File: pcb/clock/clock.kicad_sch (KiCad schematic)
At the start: 13 parts

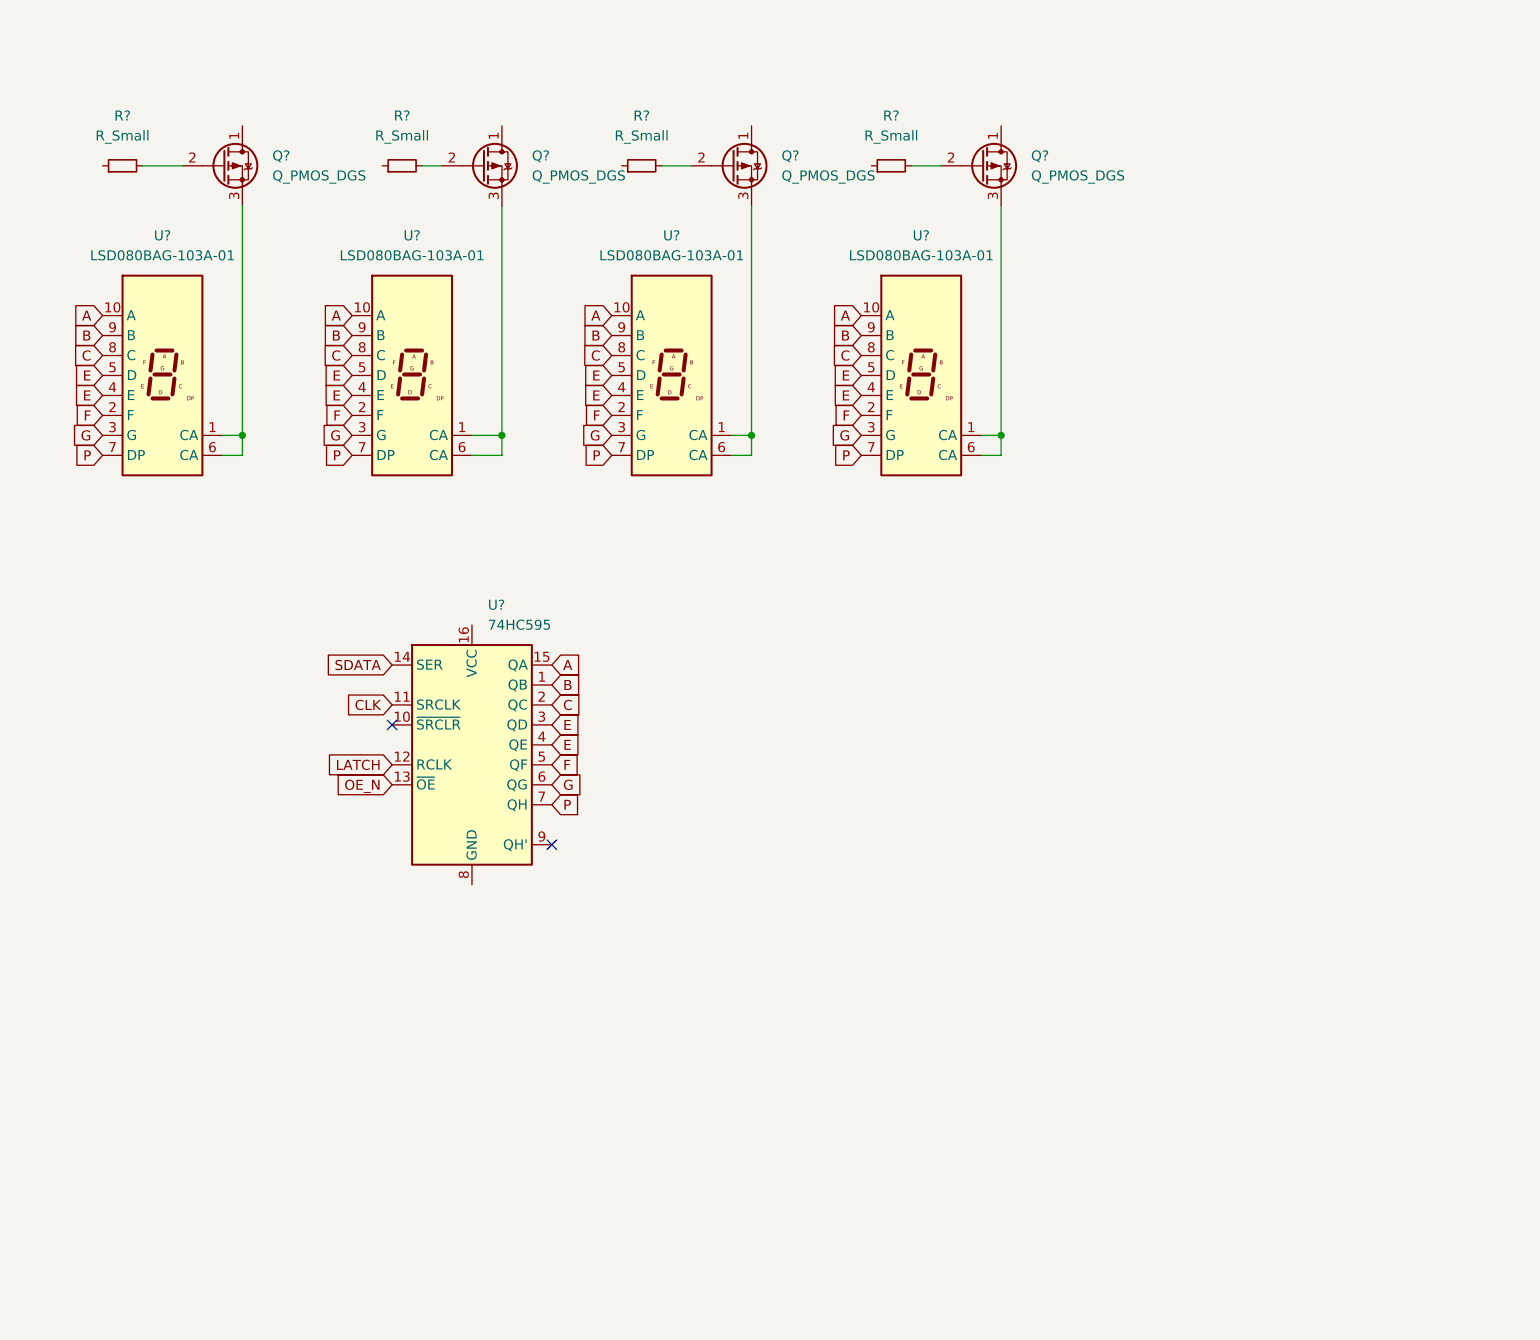
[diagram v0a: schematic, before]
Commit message: hopefully a complete schematic with footprints allocated
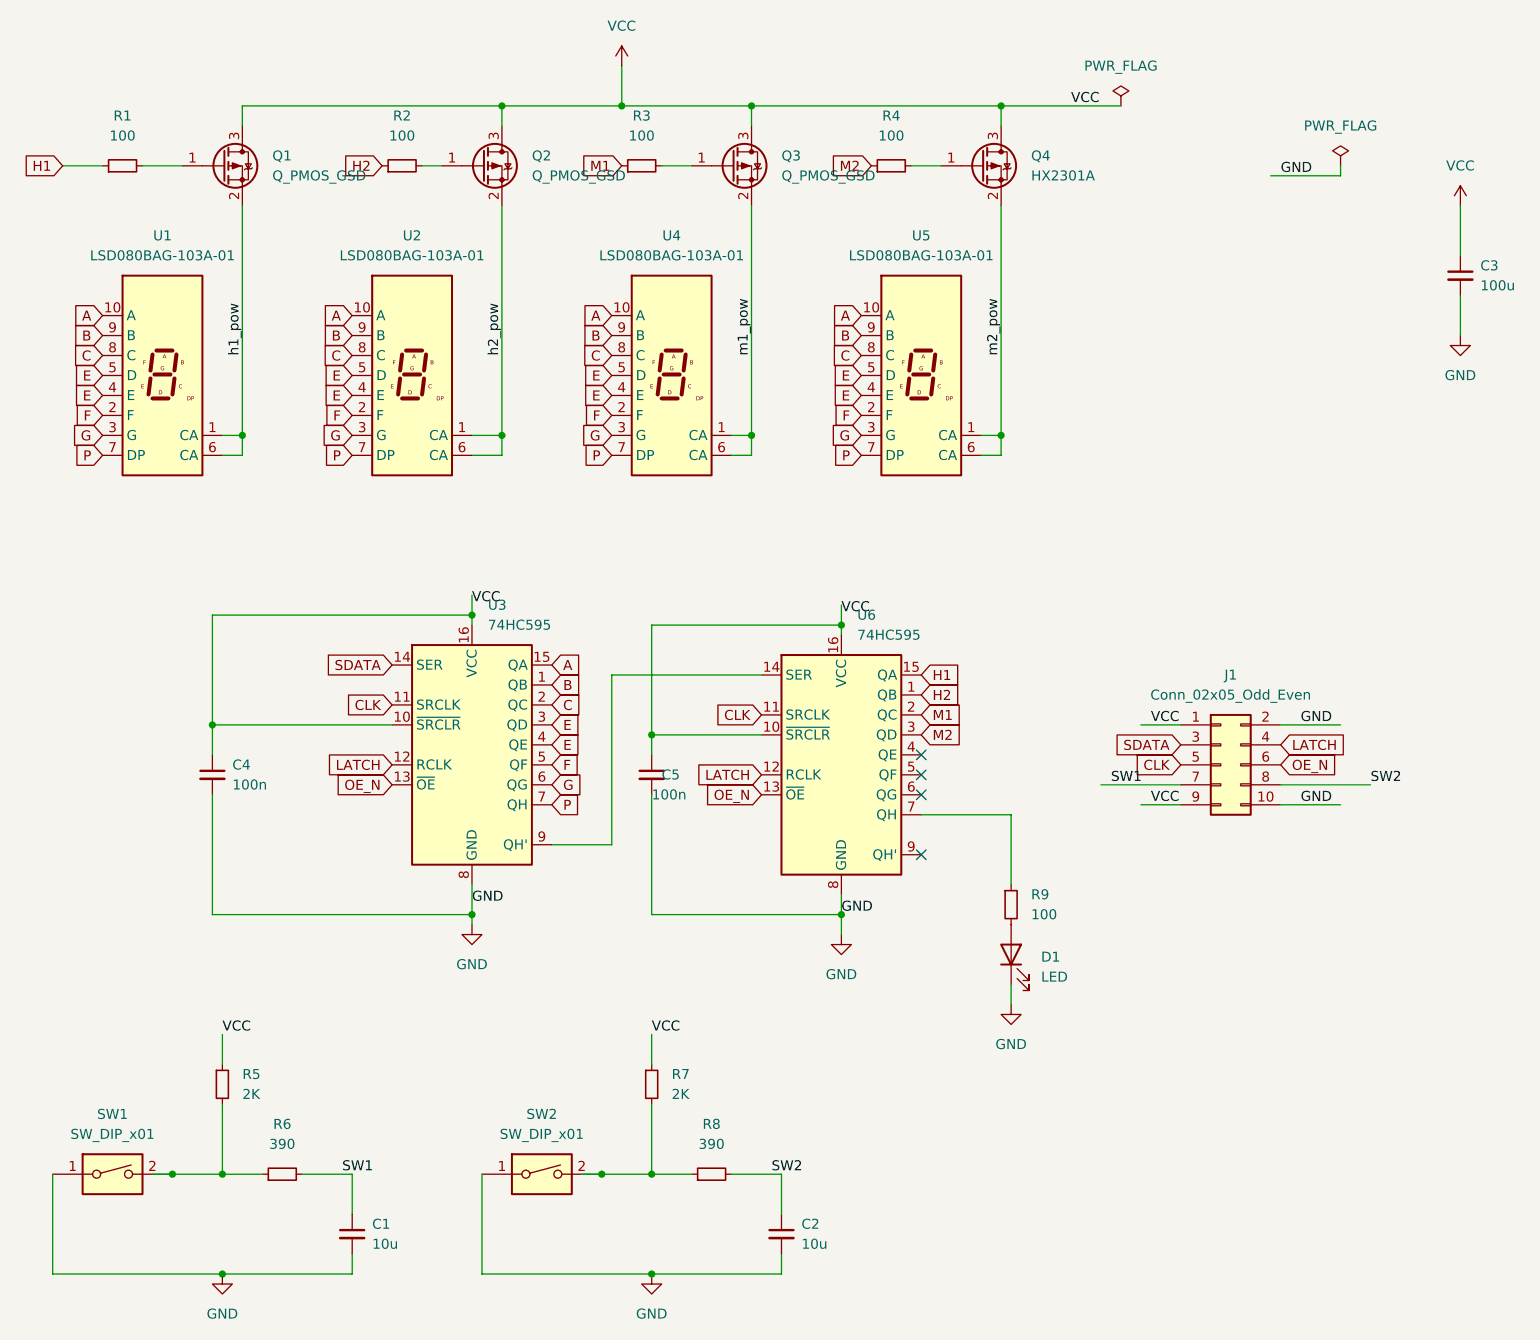
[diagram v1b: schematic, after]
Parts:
- removed Q? (x4): Q_PMOS_DGS, symbol Device:Q_PMOS_DGS
- added C1, C2: 10u, Capacitor_SMD:C_0805_2012Metric_Pad1.18x1.45mm_HandSolder, symbol Device:C_Small
- added C3: 100u, Capacitor_SMD:CP_Elec_8x10.5, symbol Device:C_Small
- added C4, C5: 100n, Capacitor_SMD:C_0805_2012Metric_Pad1.18x1.45mm_HandSolder, symbol Device:C_Small
- added D1: LED, LED_SMD:LED_0805_2012Metric_Pad1.15x1.40mm_HandSolder, symbol Device:LED
- added J1: Conn_02x05_Odd_Even, Connector_PinHeader_2.54mm:PinHeader_2x05_P2.54mm_Vertical_SMD, symbol Connector_Generic:Conn_02x05_Odd_Even
- added Q1, Q2, Q3: Q_PMOS_GSD, Package_TO_SOT_SMD:SOT-23_Handsoldering, symbol Device:Q_PMOS_GSD
- added Q4: HX2301A, Package_TO_SOT_SMD:SOT-23_Handsoldering, symbol Device:Q_PMOS_GSD
- added R5, R7: 2K, Resistor_SMD:R_0805_2012Metric_Pad1.20x1.40mm_HandSolder, symbol Device:R_Small
- added R6, R8: 390, Resistor_SMD:R_0805_2012Metric_Pad1.20x1.40mm_HandSolder, symbol Device:R_Small
- added R9: 100, Resistor_SMD:R_0805_2012Metric_Pad1.20x1.40mm_HandSolder, symbol Device:R_Small
- added SW1, SW2: SW_DIP_x01, components:SW_SPST_lcsc_c174049, symbol Switch:SW_DIP_x01
- added U6: 74HC595, Package_SO:SOIC-16_3.9x9.9mm_P1.27mm, symbol 74xx:74HC595
- R1, R2, R3, R4: renamed from R?; value R_Small -> 100; footprint (none) -> Resistor_SMD:R_0603_1608Metric_Pad0.98x0.95mm_HandSolder
- U1, U2, U4, U5: renamed from U?; footprint Display_7Segment:HDSP-7401 -> components:7SegmentLED_lsd080bag-103a
- U3: renamed from U?; footprint (none) -> Package_SO:SOIC-16_3.9x9.9mm_P1.27mm
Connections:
- net CLK: now also J1.5 (Pin_5), U6.11 (SRCLK)
- net LATCH: now also J1.4 (Pin_4), U6.12 (RCLK)
- net OE_N: now also J1.6 (Pin_6), U6.13 (~{OE})
- net SDATA: now also J1.3 (Pin_3)
- net at R2.2: now also Q2.1 (G)
- net h2_pow: now reaches U2.1 (CA), U2.6 (CA)
- net h2_pow: now also Q2.2 (S)
- net m1_pow: now reaches U4.1 (CA), U4.6 (CA)
- net m1_pow: now also Q3.2 (S)
- net M2: now reaches R4.1
- net M2: now also U6.3 (QD)
- net at R4.2: now also Q4.1 (G)
- net VCC: now reaches U3.10 (~{SRCLR})
- net VCC: now also U3.16 (VCC), C3.1, C4.1, C5.1, J1.1 (Pin_1), J1.9 (Pin_9), Q1.3 (D), Q2.3 (D), Q3.3 (D), Q4.3 (D), R5.1, R7.1, U6.10 (~{SRCLR}), U6.16 (VCC)
- net GND: now reaches U3.8 (GND)
- net GND: now also C1.2, C2.2, C3.2, C4.2, C5.2, D1.1 (K), J1.10 (Pin_10), J1.2 (Pin_2), SW1.1, SW2.1, U6.8 (GND)
- net at U3.9 (QH'): now also U6.14 (SER)
- net m2_pow: now reaches U5.1 (CA), U5.6 (CA)
- net m2_pow: now also Q4.2 (S)
- net at R1.2: now also Q1.1 (G)
- net h1_pow: now reaches U1.1 (CA), U1.6 (CA)
- net h1_pow: now also Q1.2 (S)
- net H2: now reaches R2.1
- net H2: now also U6.1 (QB)
- net M1: now reaches R3.1
- net M1: now also U6.2 (QC)
- net at R3.2: now also Q3.1 (G)
- net H1: now reaches R1.1
- net H1: now also U6.15 (QA)
- new net: R7.2, R8.1, SW2.2
- new net: D1.2 (A), R9.2
- new net: R9.1, U6.7 (QH)
- new net: R5.2, R6.1, SW1.2
- new net SW1: C1.1, J1.7 (Pin_7), R6.2
- new net SW2: C2.1, J1.8 (Pin_8), R8.2
- no-connect marks 2 -> 4

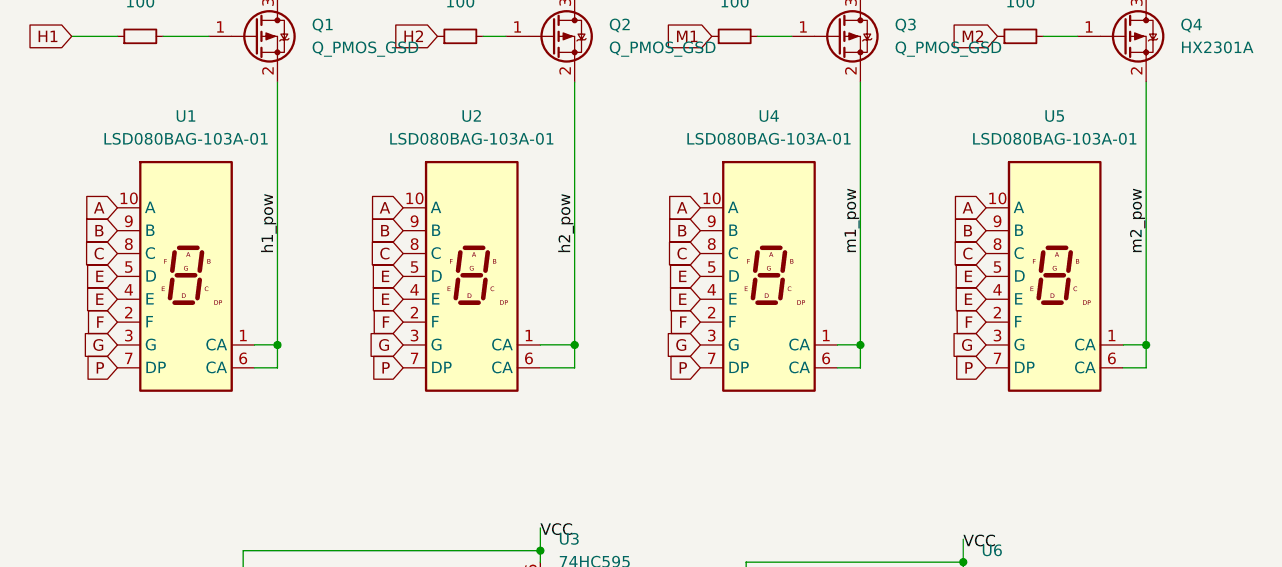
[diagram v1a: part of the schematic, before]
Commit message: fixed wrong symbol for the 7seg, D leg was shorted with E leg, added elephant logo. placement of 7 seg n switches
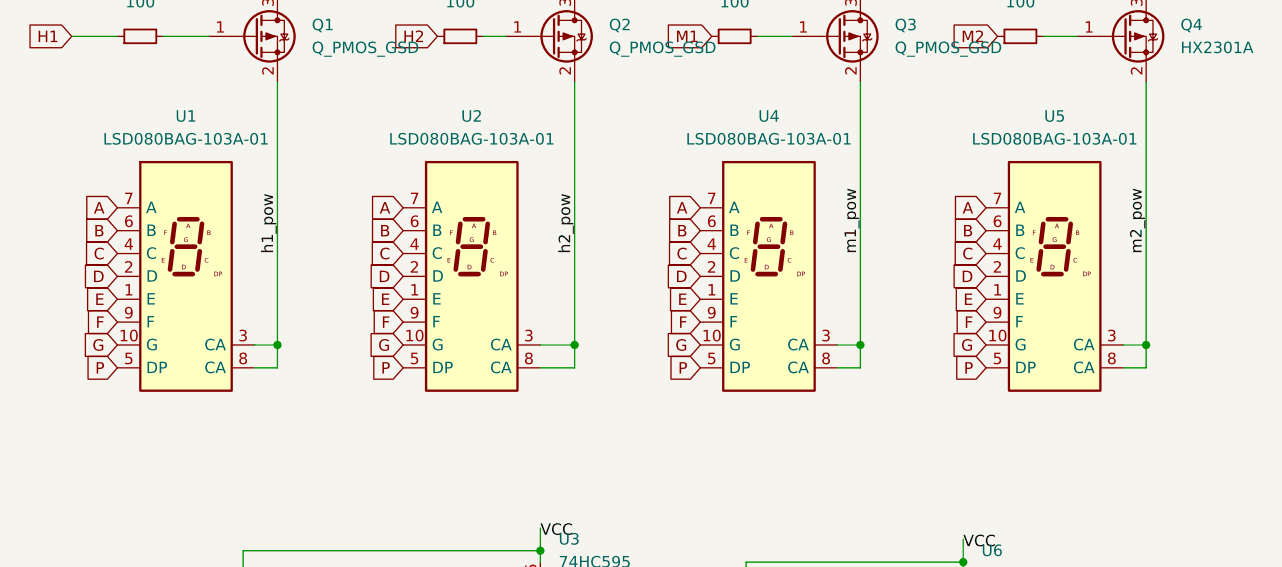
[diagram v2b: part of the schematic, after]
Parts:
- removed U1, U2, U4, U5: LSD080BAG-103A-01, components:7SegmentLED_lsd080bag-103a, symbol Display_Character:HDSP-7401
- added U1, U2, U4, U5: LSD080BAG-103A-01, components:7SegmentLED_lsd080bag-103a, symbol Display_Character:KCSA02-123
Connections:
- net A: now also U1.7 (A), U2.7 (A), U4.7 (A), U5.7 (A)
- net B: now also U1.6 (B), U2.6 (B), U4.6 (B), U5.6 (B)
- net C: now also U1.4 (C), U2.4 (C), U4.4 (C), U5.4 (C)
- net E: now also U1.1 (E), U2.1 (E), U4.1 (E), U5.1 (E)
- net F: now also U1.9 (F), U2.9 (F), U4.9 (F), U5.9 (F)
- net G: now also U1.10 (G), U2.10 (G), U4.10 (G), U5.10 (G)
- net P: now also U1.5 (DP), U2.5 (DP), U4.5 (DP), U5.5 (DP)
- net h1_pow: now also U1.3 (CA), U1.8 (CA)
- net h2_pow: now also U2.3 (CA), U2.8 (CA)
- net m1_pow: now also U4.3 (CA), U4.8 (CA)
- net m2_pow: now also U5.3 (CA), U5.8 (CA)
- new net D: U1.2 (D), U2.2 (D), U4.2 (D), U5.2 (D)

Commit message: first complete pcb of the clock
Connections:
- net D: now also U3.3 (QD)
- net E: no longer U3.3 (QD)
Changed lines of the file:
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@@
     )
   )
-  (global_label "E" (shape input) (at 132.08 115.57 0) (fields_autoplaced)
+  (global_label "D" (shape input) (at 132.08 115.57 0) (fields_autoplaced)
     (effects (font (size 1.27 1.27)) (justify left))
-    (property "Intersheet References" "${INTERSHEET_REFS}" (id 0) (at 135.6421 115.4906 0)
+    (property "Intersheet References" "${INTERSHEET_REFS}" (id 0) (at 135.7631 115.4906 0)
       (effects (font (size 1.27 1.27)) (justify left) hide)
     )
